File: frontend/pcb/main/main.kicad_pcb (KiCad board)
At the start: 2 copper layers, 27 parts, among them J1 Ext, J2 Conn_01x02, J3 Conn_01x09, J4 Debug, J5 RS485, Q1 MMBT3904, Q2 MMBT3904, U1 ESP32-WROOM-32, U2 AP1117-33, U3 MAX485E

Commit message: Add buttons.
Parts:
- added J6: Conn_01x04, Connector_JST:JST_XH_B4B-XH-A_1x04_P2.50mm_Vertical, F.Cu at (49.9, 53.2)
- added J7: Conn_01x02, Connector_JST:JST_XH_B2B-XH-A_1x02_P2.50mm_Vertical, F.Cu at (53.9, 61.0)
- added R6: 1k, Resistor_SMD:R_0603_1608Metric, F.Cu at (48.4, 58.8)
- added R7: 1k, Resistor_SMD:R_0603_1608Metric, F.Cu at (48.4, 61.4)
- added R8: 1k, Resistor_SMD:R_0603_1608Metric, F.Cu at (48.4, 63.9)
- added R9: 1k, Resistor_SMD:R_0603_1608Metric, F.Cu at (48.4, 66.4)
- J4: footprint Connector_JST:JST_XH_B6B-XH-A_1x06_P2.50mm_Vertical -> Connector_PinHeader_2.54mm:PinHeader_1x06_P2.54mm_Vertical
- moved J4 36.8 mm to (74.7, 93.5), turned to 90 degrees
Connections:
- U1 pad 6: unconnected-(U1-IO34-Pad6) -> B3
- U1 pad 7: unconnected-(U1-IO35-Pad7) -> B4
- U1 pad 8: unconnected-(U1-IO32-Pad8) -> B1
- U1 pad 9: unconnected-(U1-IO33-Pad9) -> B2

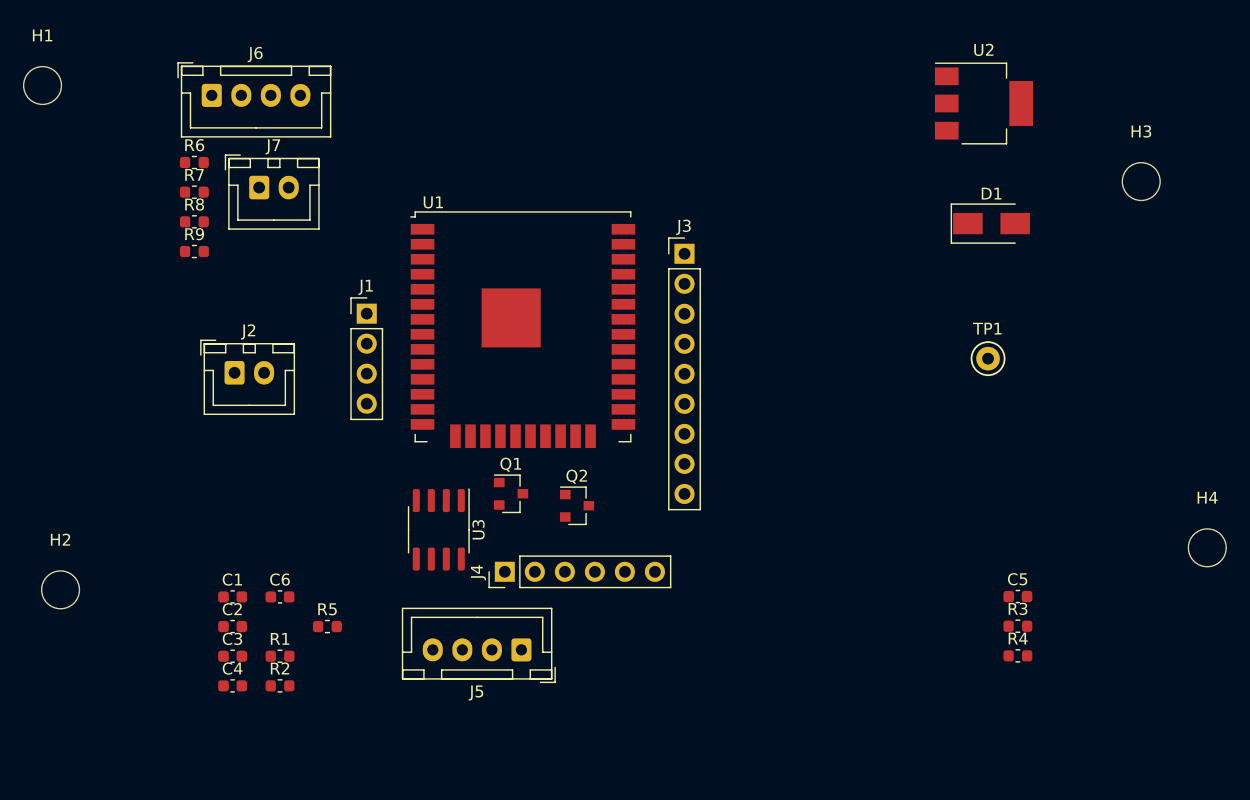
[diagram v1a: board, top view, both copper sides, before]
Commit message: Place mounting holes.
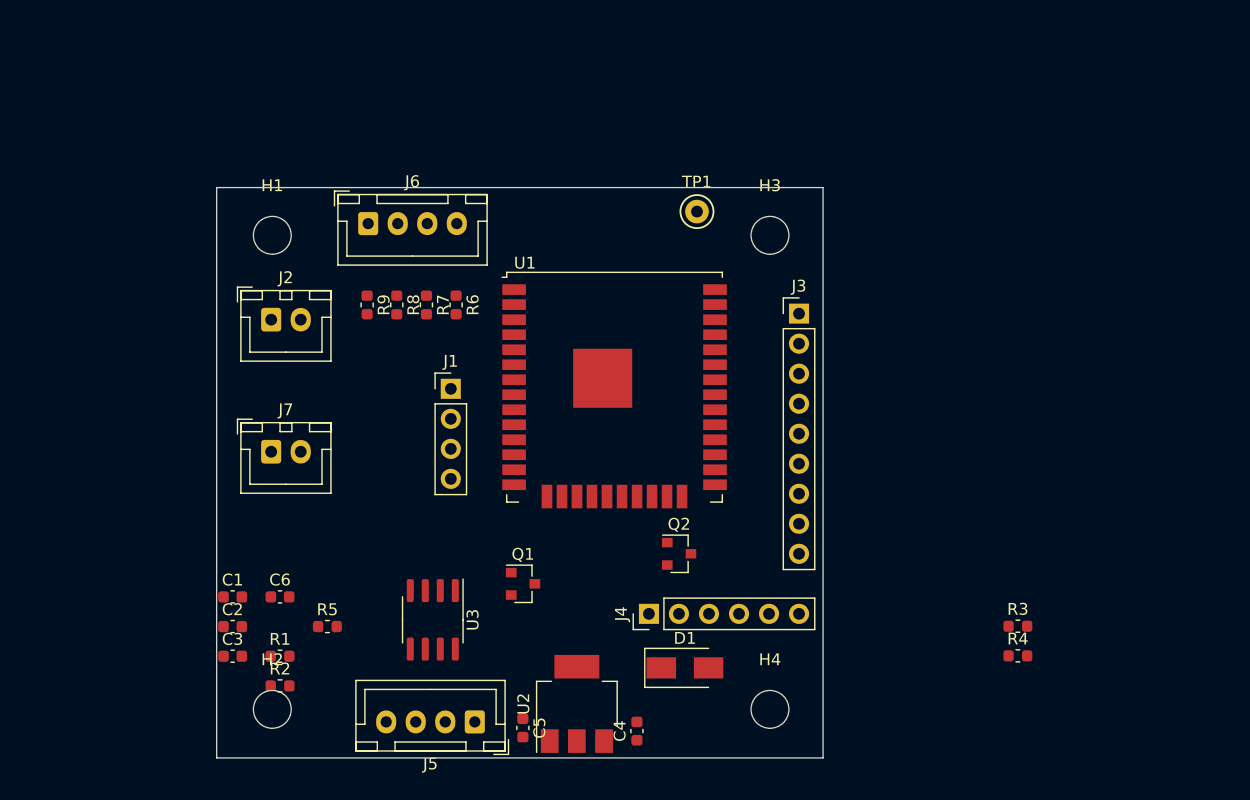
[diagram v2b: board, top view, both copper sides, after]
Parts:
- moved U2 61.4 mm to (80.8, 104.6), turned to 90 degrees
- moved D1 45.7 mm to (89.9, 101.6)
- moved C5 43.3 mm to (76.2, 106.7), turned to -90 degrees
- moved H4 39.4 mm to (97.1, 105.1)
- moved C4 34.4 mm to (85.9, 106.9), turned to 90 degrees
- moved H3 31.7 mm to (97.1, 65.0)
- moved TP1 27.6 mm to (90.9, 63.0)
- moved R6 25.2 mm to (70.6, 70.9), turned to -90 degrees
- moved H1 23.2 mm to (55.0, 65.0)
- moved J7 22.4 mm to (54.9, 83.3)
- moved R7 21.8 mm to (68.0, 70.9), turned to -90 degrees
- moved H2 20.6 mm to (55.0, 105.1)
- moved R8 18.5 mm to (65.5, 70.9), turned to -90 degrees
- moved J6 17.1 mm to (63.1, 64.0)
- moved R9 15.3 mm to (63.0, 70.9), turned to -90 degrees
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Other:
- board outline added: 51.3 x 48.3 mm

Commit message: Finish relay board.
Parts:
- J2: value Conn_01x02 -> Conn_01x03; footprint Connector_JST:JST_XH_B2B-XH-A_1x02_P2.50mm_Vertical -> Connector_PinHeader_2.54mm:PinHeader_1x03_P2.54mm_Vertical
- moved R3 49.4 mm to (68.8, 101.1), turned to 180 degrees
- moved R4 44.4 mm to (74.7, 91.2), turned to 90 degrees
- moved C2 43.6 mm to (94.5, 90.2), turned to -90 degrees
- moved R2 35.7 mm to (90.1, 94.0)
- moved C1 33.1 mm to (73.2, 70.4), turned to 90 degrees
- moved C3 32.9 mm to (82.8, 90.2), turned to 90 degrees
- moved R1 29.2 mm to (84.0, 94.0)
- moved R5 18.4 mm to (76.7, 91.2), turned to -90 degrees
- moved Q1 15.7 mm to (91.4, 90.4), turned to 90 degrees
- moved C6 13.7 mm to (69.1, 98.3), turned to -90 degrees
- moved J2 12.9 mm to (55.0, 85.0)
- moved J7 9.20 mm to (54.4, 74.1), turned to 90 degrees
- moved U3 4.19 mm to (72.6, 96.5)
- moved Q2 3.88 mm to (85.9, 90.4), turned to 90 degrees
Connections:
- J2 pad 1: Relay -> GND
- J2 pad 2: GND -> Relay
- U1 pad 6: B3 -> B1
- U1 pad 7: B4 -> B2
- U1 pad 8: B1 -> B3
- U1 pad 9: B2 -> B4
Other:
- board size 51.3 x 48.3 mm -> 50.3 x 48.3 mm

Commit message: Do first routing pass.
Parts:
- moved R1 8.92 mm to (93.0, 94.0)
- moved R2 5.87 mm to (96.0, 94.0)
- moved J1 3.56 mm to (70.1, 81.5)
- moved R6 0.56 mm to (70.6, 70.3)
- moved R7 0.56 mm to (68.0, 70.3)
- moved R8 0.56 mm to (65.5, 70.3)
- moved R9 0.56 mm to (63.0, 70.3)
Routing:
- net GND: track 0.00 -> 193.4 mm, vias 0 -> 5
- net +3V3: track 0.00 -> 94.3 mm, vias 0 -> 7
- net +5V: track 0.00 -> 66.6 mm, vias 0 -> 1
- net Relay: track 0.00 -> 42.3 mm, vias 0 -> 1
- net TX485: track 0.00 -> 30.1 mm, vias 0 -> 2
- net /MCU_TX0: track 0.00 -> 27.6 mm, vias 0 -> 2
- net RESET: track 0.00 -> 26.6 mm
- net Display_SDO: track 0.00 -> 26.2 mm
- net B4: track 0.00 -> 24.9 mm
- net /MCU_RX0: track 0.00 -> 24.7 mm, vias 0 -> 2
- net Display_SDI: track 0.00 -> 23.0 mm, vias 0 -> 2
- net DTR: track 0.00 -> 22.6 mm, vias 0 -> 2
- net B3: track 0.00 -> 20.7 mm
- net RX485: track 0.00 -> 19.7 mm, vias 0 -> 2
- net B2: track 0.00 -> 17.7 mm
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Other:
- board text added: "."
- board text added: "ACS frontend"
- board text added: "Buttons"
- board text added: "Debug"
- board text added: "Display"
- board text added: "Ext"
- board text added: "G"
- board text added: "Leave"
- board text added: "https://github.com/bullestock/acsv2"

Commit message: Final adjustments, order.
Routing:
- net +3V3: track 94.3 -> 114.2 mm
- net +5V: track 66.6 -> 70.5 mm
- net GND: track 193.4 -> 195.7 mm
- added copper zone on B.Cu, net GND
- added copper zone on F.Cu, net GND
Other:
- board size 50.3 x 48.3 mm -> 51 x 49 mm

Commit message: Remove capacitors.
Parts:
- removed C2, C3: 100n, Capacitor_SMD:C_0603_1608Metric
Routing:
- net GND: track 195.7 -> 188.4 mm
- net BOOT: track 6.90 -> 3.77 mm

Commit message: Add R10.
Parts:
- added R10: 10k, Resistor_SMD:R_0603_1608Metric, F.Cu at (60.3, 71.1)
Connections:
- J7 pad 2: B4 -> Net-(J7-Pin_2)
- R9 pad 2: B4 -> Net-(J7-Pin_2)
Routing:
- net Net-(J7-Pin_2): track 0.00 -> 9.52 mm
- net B4: track 24.9 -> 19.5 mm
- net +5V: track 70.5 -> 69.3 mm

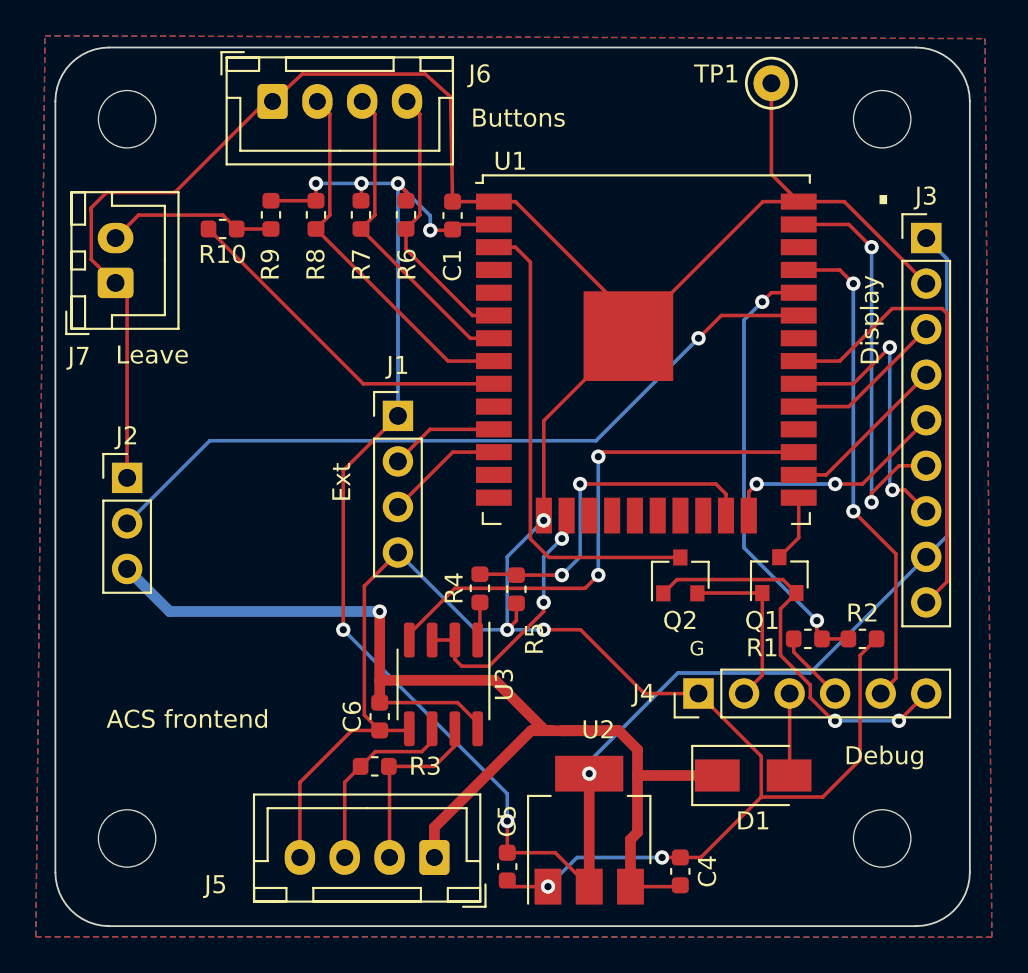
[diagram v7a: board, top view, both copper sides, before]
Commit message: Integrate relay board components into main board. Add switches and LEDs.
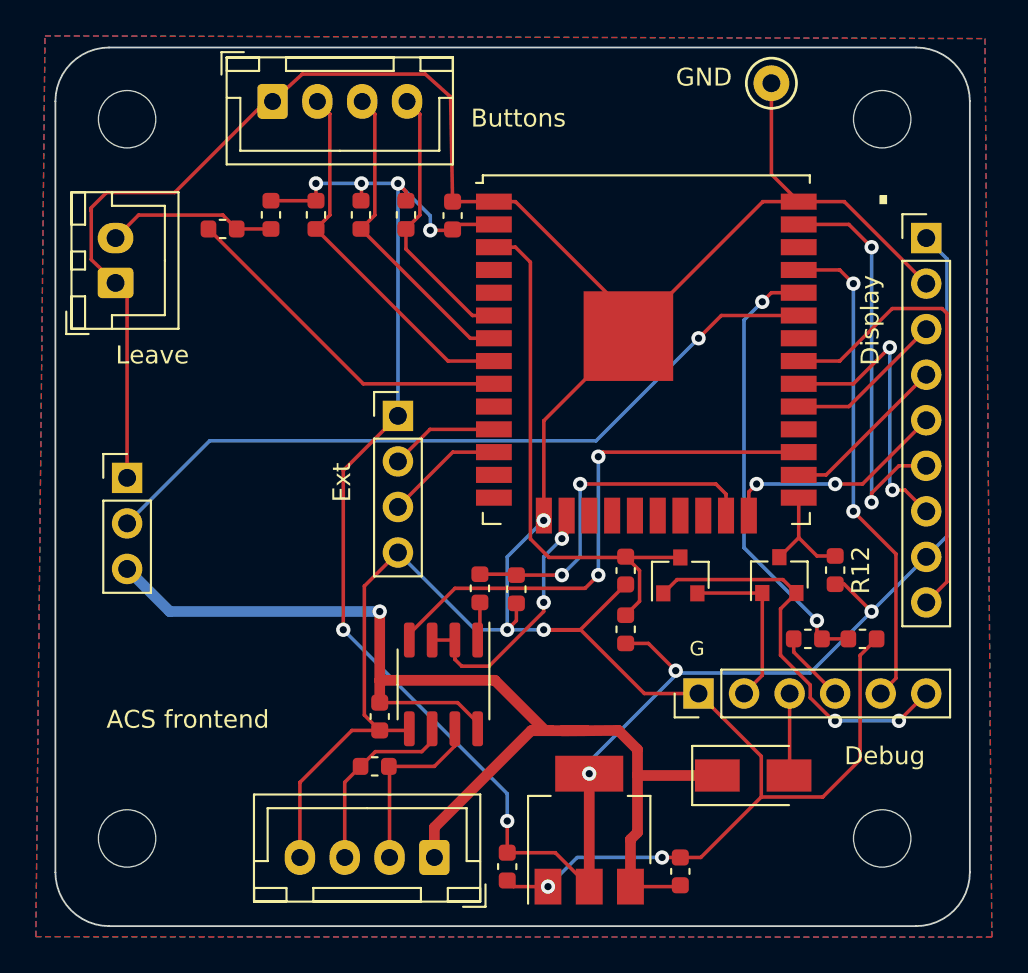
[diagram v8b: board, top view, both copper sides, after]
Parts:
- added C2: 100n, Capacitor_SMD:C_0603_1608Metric, F.Cu at (82.8, 90.2)
- added R11: 10k, Resistor_SMD:R_0603_1608Metric, F.Cu at (82.8, 93.4)
- added R12: 10k, Resistor_SMD:R_0603_1608Metric, F.Cu at (94.5, 90.1)
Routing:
- net +3V3: track 114.2 -> 120.3 mm, vias 7 -> 9
- net GND: track 188.4 -> 194.1 mm
- net RESET: track 26.6 -> 30.5 mm
- net BOOT: track 3.77 -> 6.22 mm
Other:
- board text added: "GND"
